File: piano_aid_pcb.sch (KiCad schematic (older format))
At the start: 28 parts, among them J1 Barrel_Jack_MountingPin, J2 796644-3, J3 DIN-5_180degree, J4 Conn_01x06_Female, J5 Micro_SD_Card_Det, J6 Conn_01x07_Female, U1 317030213, U2 6N138, U3 74AHCT1G125W5-7, U4 AZ1117-3.3

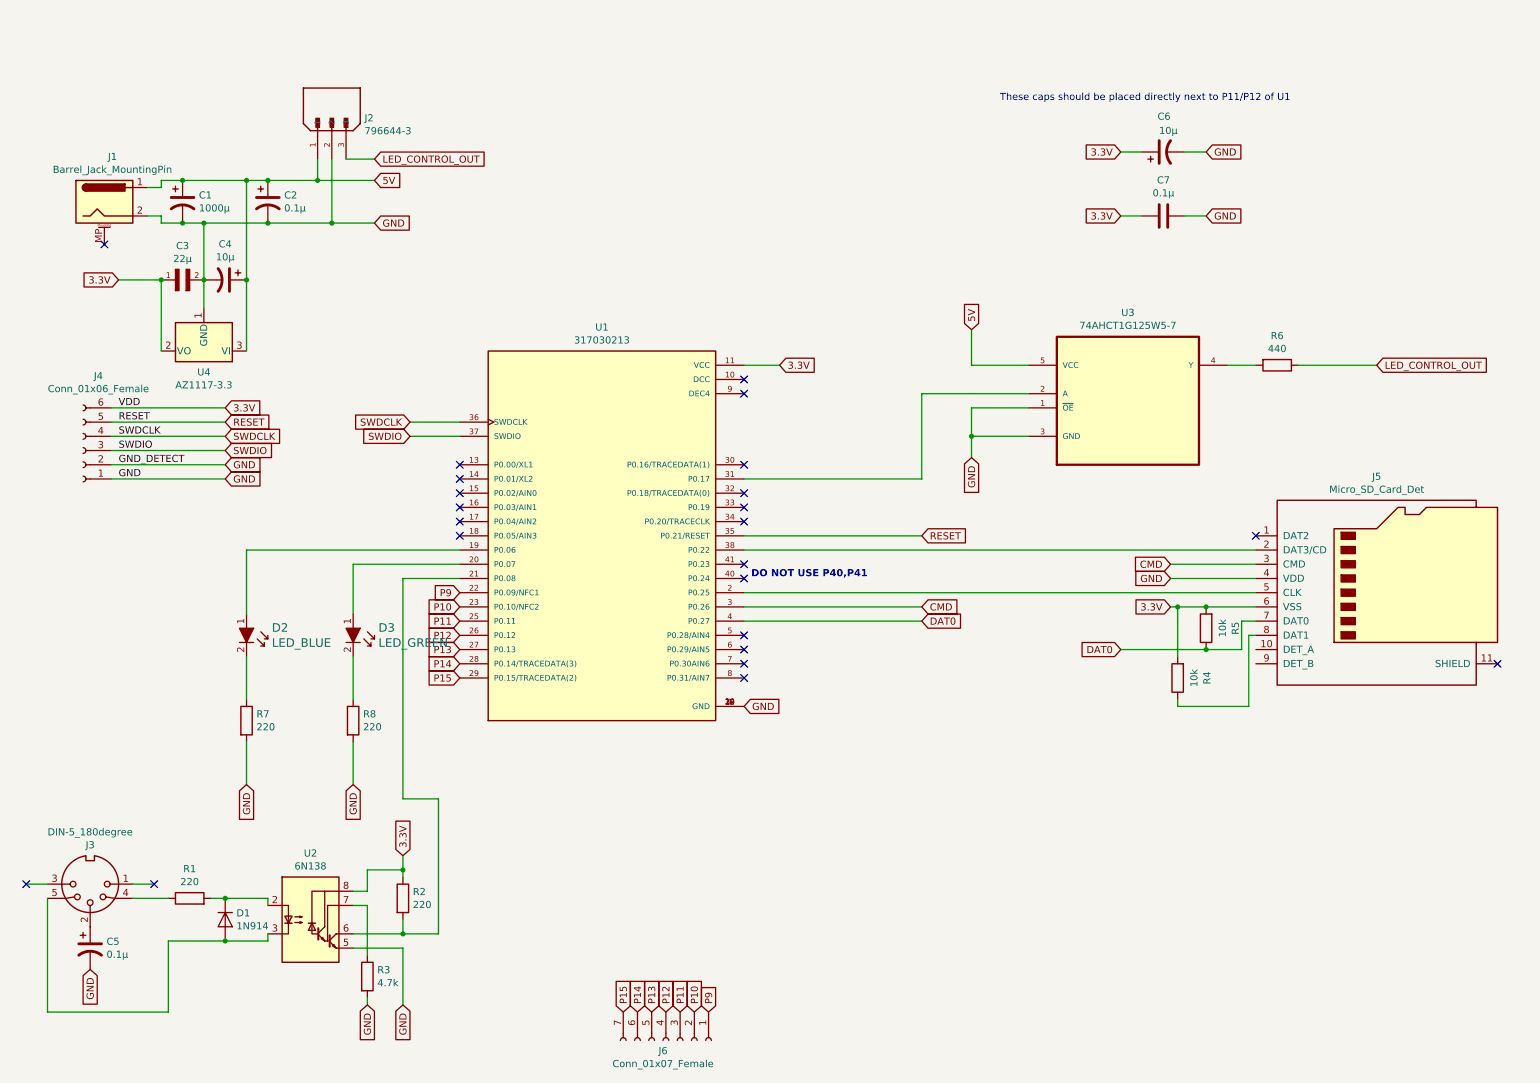
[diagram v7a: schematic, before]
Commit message: Completely re-traced and layed out board. Presenting PCB V2
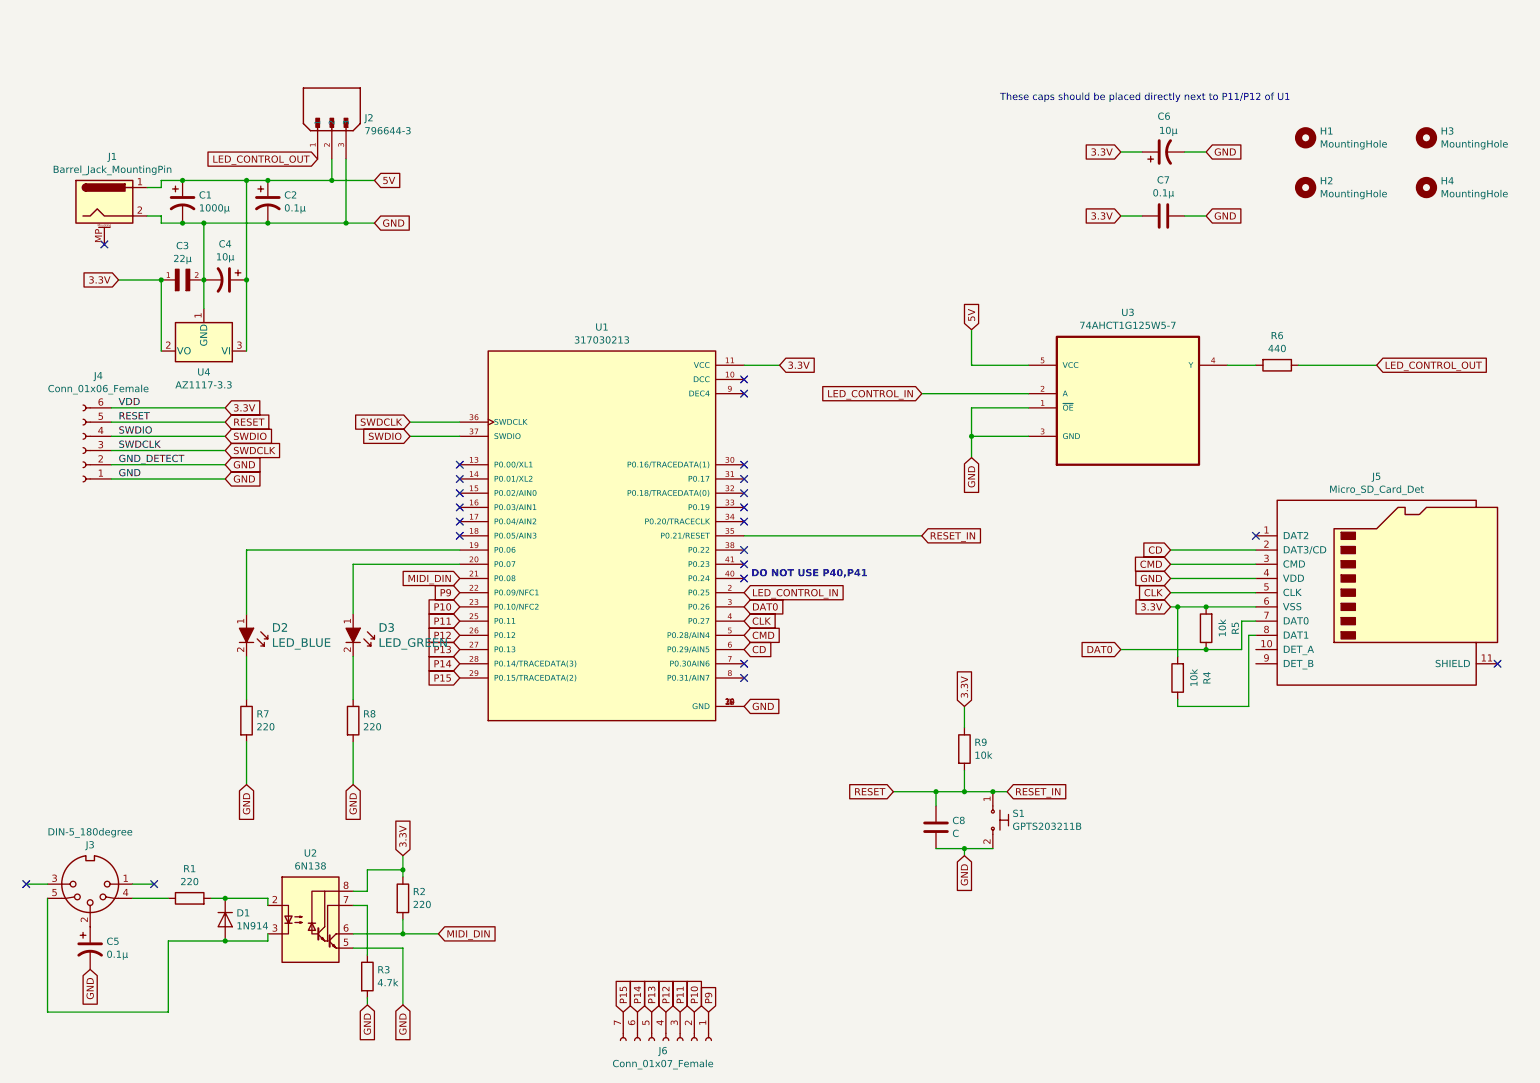
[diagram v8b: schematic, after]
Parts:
- added C8: C, Capacitor_SMD:C_0805_2012Metric_Pad1.15x1.40mm_HandSolder, symbol Device:C
- added H1, H2, H3, H4: MountingHole, MountingHole:MountingHole_2.2mm_M2, symbol Mechanical:MountingHole
- added R9: 10k, Resistor_SMD:R_0805_2012Metric_Pad1.15x1.40mm_HandSolder, symbol Device:R
- added S1: GPTS203211B, 4-1437565-1:SW_4-1437565-1, symbol dk_Pushbutton-Switches:GPTS203211B
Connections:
- net 3.3V: now also R9.1
- net 5V: now also J2.2; no longer J2.1
- net CMD: now also U1.5 (P0.28/AIN4); no longer U1.3 (P0.26)
- net DAT0: now also U1.3 (P0.26); no longer U1.4 (P0.27)
- net GND: now also J2.3, C8.2, S1.2; no longer J2.2
- net LED_CONTROL_OUT: now also J2.1; no longer J2.3
- net RESET: now also C8.1, R9.2, S1.1
- net SWDCLK: now also J4.3 (Pin_3); no longer J4.4 (Pin_4)
- net SWDIO: now also J4.4 (Pin_4); no longer J4.3 (Pin_3)
- net MIDI_DIN: now reaches R2.2, U1.21 (P0.08), U2.6 (VO2)
- net CLK: now reaches J5.5 (CLK)
- net CLK: now also U1.4 (P0.27); no longer U1.2 (P0.25)
- net at U1.31 (P0.17): no longer U3.2 (A)
- net at U1.38 (P0.22): no longer J5.2 (DAT3/CD)
- net CD: now reaches U1.6 (P0.29/AIN5)
- net CD: now also J5.2 (DAT3/CD)
- new net LED_CONTROL_IN: U1.2 (P0.25), U3.2 (A)
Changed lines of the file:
@@
 Title "Interactive Piano Aid"
 Date "2021-09-07"
-Rev "v01"
+Rev "v02"
 Comp ""
 Comment1 ""
@@
 Text Label 1250 2800 0    50   ~ 0
 VDD
+Text Label 1250 3100 0    50   ~ 0
+SWDCLK
 Text Label 1250 3000 0    50   ~ 0
-SWDCLK
-Text Label 1250 3100 0    50   ~ 0
 SWDIO
 Wire Wire Line
@@
 	8650 4200 8700 4200
 Connection ~ 8900 4200
-Wire Wire Line
-	9250 3800 5650 3800
 NoConn ~ 9250 3700
-Wire Wire Line
-	9250 4100 5650 4100
 Wire Wire Line
 	9150 4500 8900 4500
@@
 	1700 1200 2150 1200
 Wire Wire Line
-	2650 1200 3050 1200
-Connection ~ 2650 1200
-Wire Wire Line
-	2750 1500 3050 1500
-Connection ~ 2750 1500
-Wire Wire Line
-	5650 3300 6900 3300
-Wire Wire Line
 	9050 2500 9250 2500
 Wire Wire Line
@@
 LED_CONTROL_OUT
 Text GLabel 6900 3700 2    50   Input ~ 0
-RESET
+RESET_IN
 Text GLabel 2000 2900 2    50   Input ~ 0
 RESET
@@
 $EndComp
 Connection ~ 2300 1200
-Wire Wire Line
-	2300 1200 2650 1200
 Connection ~ 2300 1500
-Wire Wire Line
-	2300 1500 2750 1500
 Text GLabel 7250 3150 3    50   Input ~ 0
 GND
@@
 Wire Wire Line
 	2150 5150 2150 5450
-Text GLabel 3050 1050 2    50   Input ~ 0
-LED_CONTROL_OUT
-Wire Wire Line
-	2850 1050 3050 1050
 NoConn ~ 5650 3200
 NoConn ~ 5650 3400
 NoConn ~ 5650 3500
 NoConn ~ 5650 3600
-NoConn ~ 5650 4400
-NoConn ~ 5650 4500
+NoConn ~ 5650 3300
+NoConn ~ 5650 3800
 NoConn ~ 5650 4600
 NoConn ~ 5650 4700
@@
 Wire Wire Line
 	8650 3900 9250 3900
-Wire Wire Line
-	5650 4200 6900 4200
-Text GLabel 6900 4200 2    50   Input ~ 0
+Text GLabel 5650 4400 2    50   Input ~ 0
 CMD
 Text GLabel 8300 4500 0    50   Input ~ 0
 DAT0
-Wire Wire Line
-	5650 4300 6900 4300
-Text GLabel 6900 4300 2    50   Input ~ 0
+Text GLabel 5650 4200 2    50   Input ~ 0
 DAT0
 NoConn ~ 5650 3900
@@
 Text GLabel 3300 3000 0    50   Input ~ 0
 SWDIO
+Text GLabel 2000 3000 2    50   Input ~ 0
+SWDIO
 Text GLabel 2000 3100 2    50   Input ~ 0
-SWDIO
-Text GLabel 2000 3000 2    50   Input ~ 0
 SWDCLK
 Wire Wire Line
@@
 	6900 2700 7650 2700
 Wire Wire Line
-	6900 2700 6900 3300
-Wire Wire Line
 	7650 2800 7250 2800
 Wire Wire Line
@@
 	0    -1   -1   0
 $EndComp
-Wire Wire Line
-	2650 1050 2650 1200
-Wire Wire Line
-	2750 1050 2750 1500
 Text GLabel 3650 4100 0    50   Input ~ 0
 P9
@@
 Text GLabel 3650 4700 0    50   Input ~ 0
 P15
-Wire Wire Line
-	3250 4000 3250 5550
-Wire Wire Line
-	3250 5550 3500 5550
-Wire Wire Line
-	3500 5550 3500 6500
-Wire Wire Line
-	3250 4000 3650 4000
 Text GLabel 5400 7050 1    50   Input ~ 0
 P9
@@
 	0    1    1    0
 $EndComp
+Text GLabel 2650 1050 0    50   Input ~ 0
+LED_CONTROL_OUT
+Text GLabel 7500 5500 2    50   Input ~ 0
+RESET_IN
+$Comp
+L Device:R R9
+U 1 1 61563F75
+P 7200 5200
+F 0 "R9" H 7270 5246 50  0000 L CNN
+F 1 "10k" H 7270 5155 50  0000 L CNN
+F 2 "Resistor_SMD:R_0805_2012Metric_Pad1.15x1.40mm_HandSolder" V 7130 5200 50  0001 C CNN
+F 3 "~" H 7200 5200 50  0001 C CNN
+	1    7200 5200
+	1    0    0    -1
+$EndComp
+Text GLabel 7200 4900 1    50   Input ~ 0
+3.3V
+$Comp
+L Device:C C8
+U 1 1 61564E4F
+P 7000 5750
+F 0 "C8" H 7115 5796 50  0000 L CNN
+F 1 "C" H 7115 5705 50  0000 L CNN
+F 2 "Capacitor_SMD:C_0805_2012Metric_Pad1.15x1.40mm_HandSolder" H 7038 5600 50  0001 C CNN
+F 3 "~" H 7000 5750 50  0001 C CNN
+	1    7000 5750
+	1    0    0    -1
+$EndComp
+Text GLabel 7200 5950 3    50   Input ~ 0
+GND
+$Comp
+L dk_Pushbutton-Switches:GPTS203211B S1
+U 1 1 615742BF
+P 7400 5700
+F 0 "S1" V 7354 5838 50  0000 L CNN
+F 1 "GPTS203211B" V 7445 5838 50  0000 L CNN
+F 2 "4-1437565-1:SW_4-1437565-1" H 7600 5900 50  0001 L CNN
+F 3 "http://switches-connectors-custom.cwind.com/Asset/GPTS203211BR2.pdf" H 7600 6000 60  0001 L CNN
+F 4 "CW181-ND" H 7600 6100 60  0001 L CNN "Digi-Key_PN"
+F 5 "GPTS203211B" H 7600 6200 60  0001 L CNN "MPN"
+F 6 "Switches" H 7600 6300 60  0001 L CNN "Category"
+F 7 "Pushbutton Switches" H 7600 6400 60  0001 L CNN "Family"
+F 8 "http://switches-connectors-custom.cwind.com/Asset/GPTS203211BR2.pdf" H 7600 6500 60  0001 L CNN "DK_Datasheet_Link"
+F 9 "/product-detail/en/cw-industries/GPTS203211B/CW181-ND/3190590" H 7600 6600 60  0001 L CNN "DK_Detail_Page"
+F 10 "SWITCH PUSHBUTTON SPST 1A 30V" H 7600 6700 60  0001 L CNN "Description"
+F 11 "CW Industries" H 7600 6800 60  0001 L CNN "Manufacturer"
+F 12 "Active" H 7600 6900 60  0001 L CNN "Status"
+	1    7400 5700
+	0    1    1    0
+$EndComp
+Text GLabel 6700 5500 0    50   Input ~ 0
+RESET
+Wire Wire Line
+	6700 5500 7000 5500
+Connection ~ 7400 5500
+Wire Wire Line
+	7400 5500 7500 5500
+Wire Wire Line
+	7200 5350 7200 5500
+Connection ~ 7200 5500
+Wire Wire Line
+	7200 5500 7400 5500
+Wire Wire Line
+	7200 5050 7200 4900
+Wire Wire Line
+	7000 5600 7000 5500
+Connection ~ 7000 5500
+Wire Wire Line
+	7000 5500 7200 5500
+Wire Wire Line
+	7000 5900 7200 5900
+Wire Wire Line
+	7200 5950 7200 5900
+Connection ~ 7200 5900
+Wire Wire Line
+	7200 5900 7400 5900
+Wire Wire Line
+	2300 1500 2850 1500
+Wire Wire Line
+	2300 1200 2750 1200
+Wire Wire Line
+	2750 1050 2750 1200
+Connection ~ 2750 1200
+Wire Wire Line
+	2750 1200 3050 1200
+Wire Wire Line
+	2850 1050 2850 1500
+Connection ~ 2850 1500
+Wire Wire Line
+	2850 1500 3050 1500
+Text GLabel 6900 2700 0    50   Input ~ 0
+LED_CONTROL_IN
+Text GLabel 5650 4100 2    50   Input ~ 0
+LED_CONTROL_IN
+Wire Wire Line
+	9250 4100 8650 4100
+Text GLabel 8650 4100 0    50   Input ~ 0
+CLK
+Text GLabel 5650 4300 2    50   Input ~ 0
+CLK
+Text GLabel 3500 6500 2    50   Input ~ 0
+MIDI_DIN
+Text GLabel 3650 4000 0    50   Input ~ 0
+MIDI_DIN
+Text GLabel 8650 3800 0    50   Input ~ 0
+CD
+Wire Wire Line
+	8650 3800 9250 3800
+Text GLabel 5650 4500 2    50   Input ~ 0
+CD
+$Comp
+L Mechanical:MountingHole H1
+U 1 1 61691ABB
+P 9600 900
+F 0 "H1" H 9700 946 50  0000 L CNN
+F 1 "MountingHole" H 9700 855 50  0000 L CNN
+F 2 "MountingHole:MountingHole_2.2mm_M2" H 9600 900 50  0001 C CNN
+F 3 "~" H 9600 900 50  0001 C CNN
+	1    9600 900
+	1    0    0    -1
+$EndComp
+$Comp
+L Mechanical:MountingHole H3
+U 1 1 61691E1F
+P 10450 900
+F 0 "H3" H 10550 946 50  0000 L CNN
+F 1 "MountingHole" H 10550 855 50  0000 L CNN
+F 2 "MountingHole:MountingHole_2.2mm_M2" H 10450 900 50  0001 C CNN
+F 3 "~" H 10450 900 50  0001 C CNN
+	1    10450 900
+	1    0    0    -1
+$EndComp
+$Comp
+L Mechanical:MountingHole H2
+U 1 1 61692320
+P 9600 1250
+F 0 "H2" H 9700 1296 50  0000 L CNN
+F 1 "MountingHole" H 9700 1205 50  0000 L CNN
+F 2 "MountingHole:MountingHole_2.2mm_M2" H 9600 1250 50  0001 C CNN
+F 3 "~" H 9600 1250 50  0001 C CNN
+	1    9600 1250
+	1    0    0    -1
+$EndComp
+$Comp
+L Mechanical:MountingHole H4
+U 1 1 616927CC
+P 10450 1250
+F 0 "H4" H 10550 1296 50  0000 L CNN
+F 1 "MountingHole" H 10550 1205 50  0000 L CNN
+F 2 "MountingHole:MountingHole_2.2mm_M2" H 10450 1250 50  0001 C CNN
+F 3 "~" H 10450 1250 50  0001 C CNN
+	1    10450 1250
+	1    0    0    -1
+$EndComp
 $EndSCHEMATC
